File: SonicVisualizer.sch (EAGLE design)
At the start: 71 parts, among them U1 LMV324, U2 LMV324, U3 LMV324, U4 +12v, U5 +12v

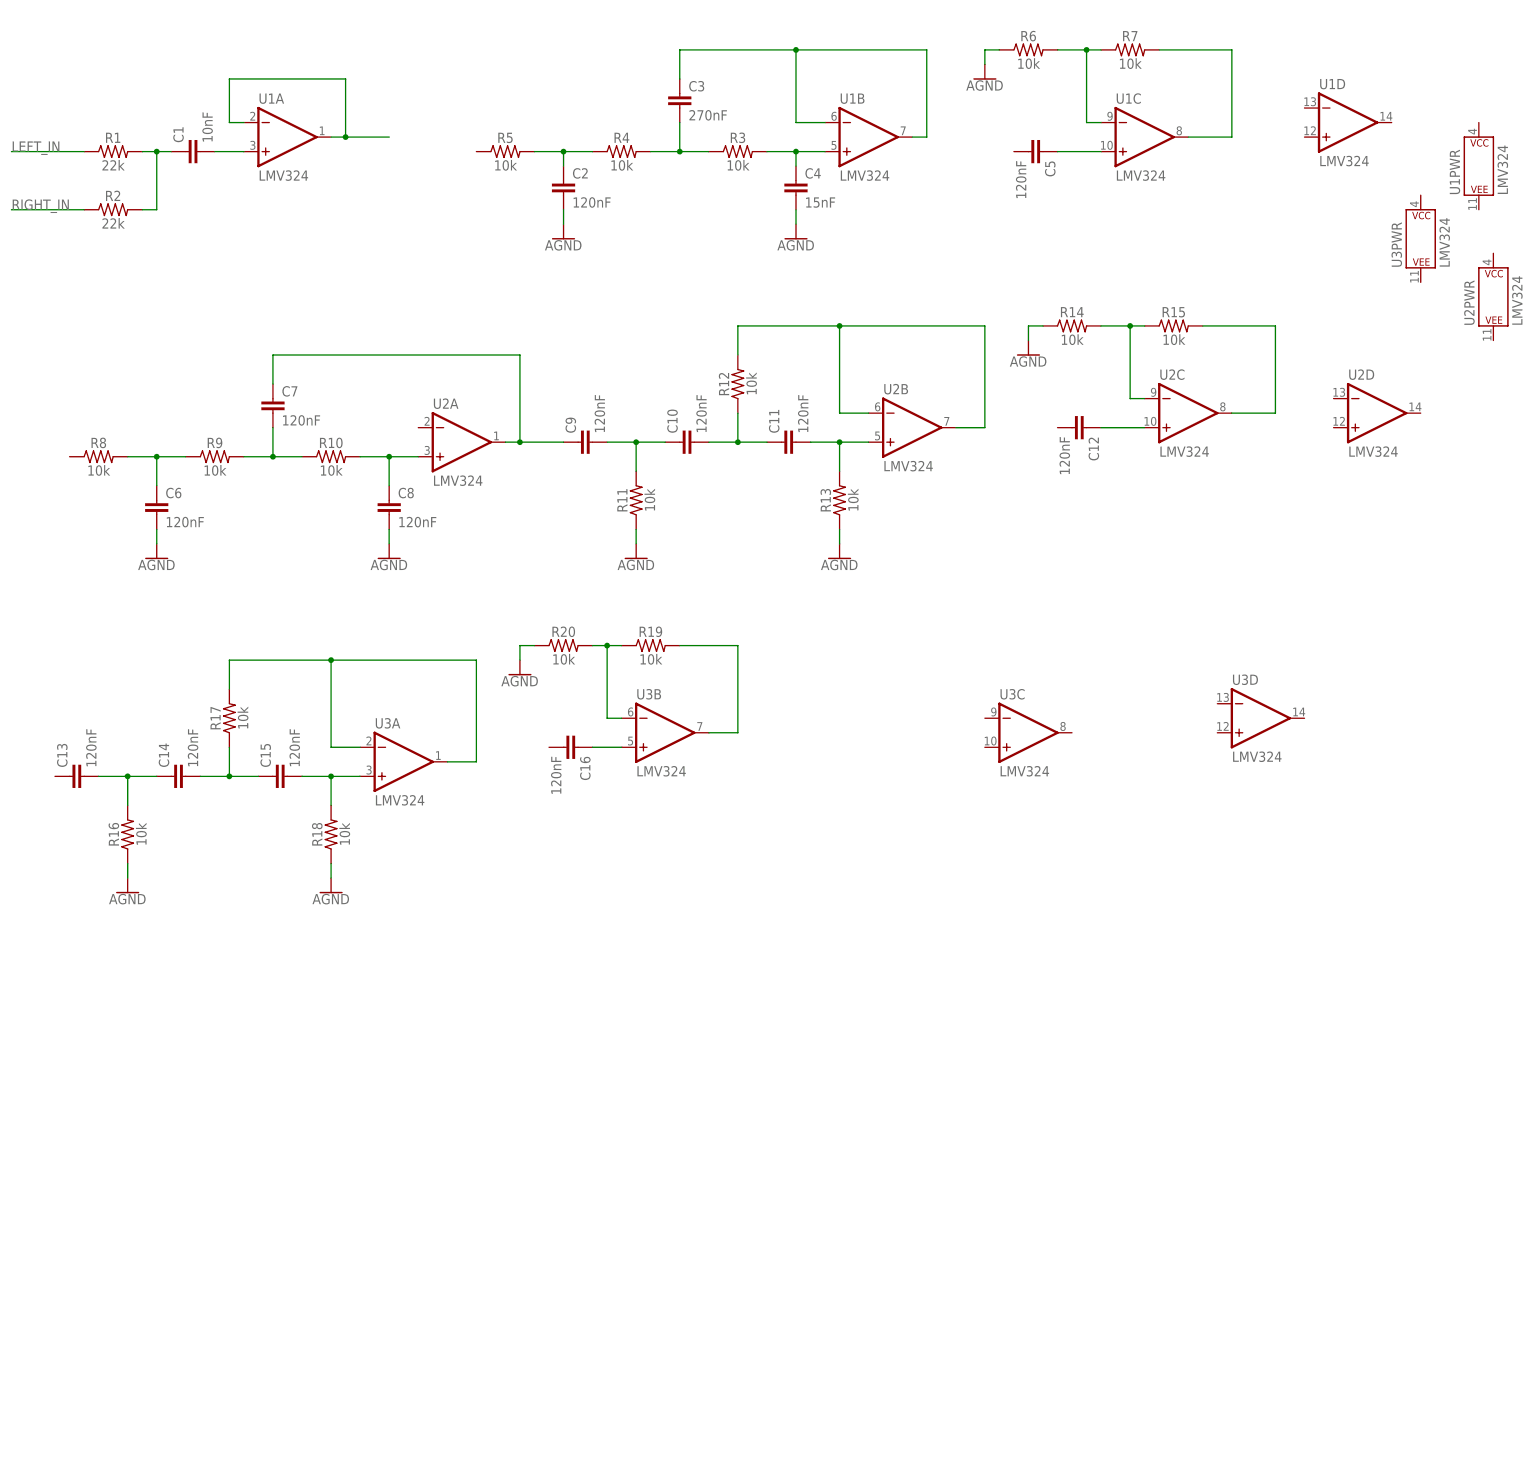
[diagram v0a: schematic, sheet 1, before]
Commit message: Compressed schematic and added envelope detect stage
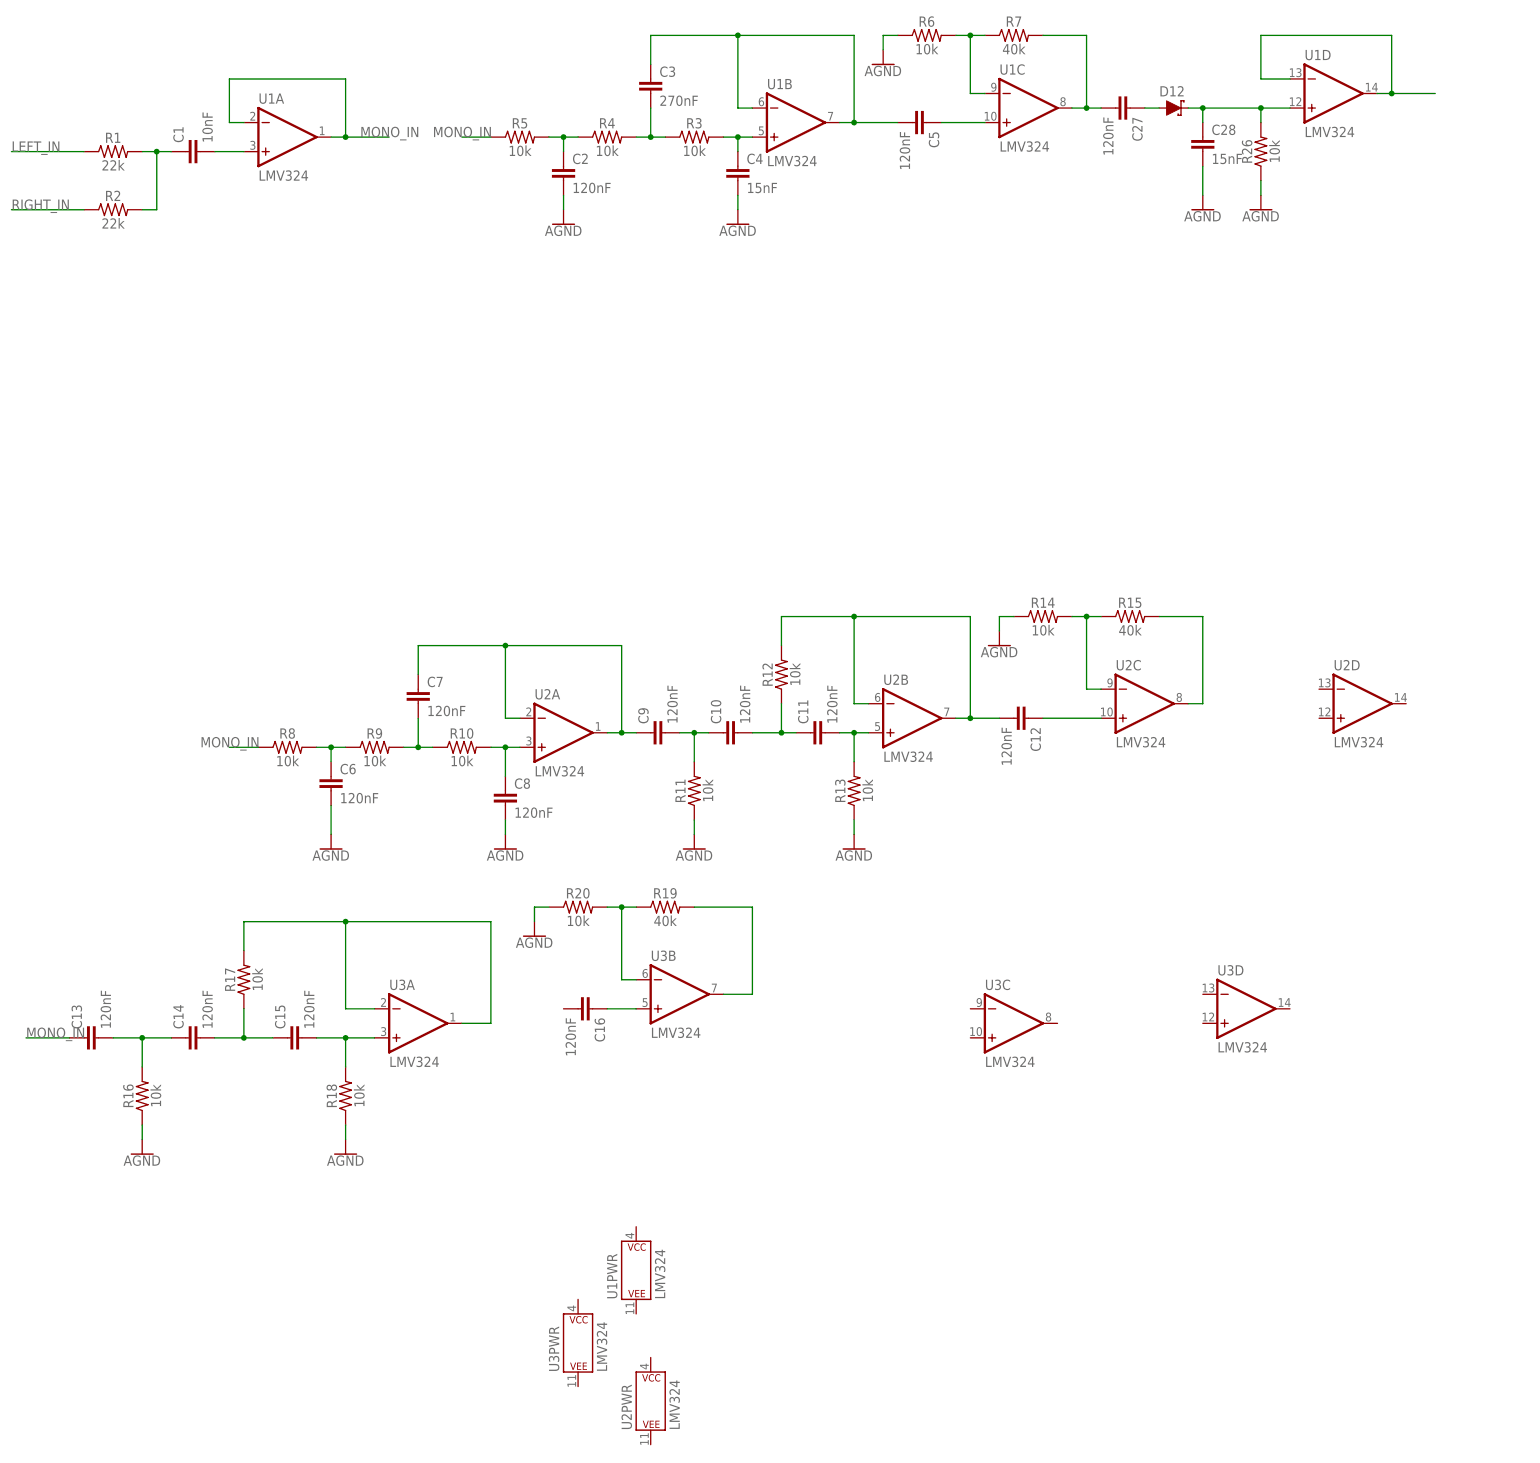
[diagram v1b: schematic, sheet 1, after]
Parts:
- added C27: 120nF, SparkFun-Capacitors:0.1UF-0603-25V-(+80/-20%)
- added C28: 15nF, SparkFun-Capacitors:0.1UF-0603-25V-(+80/-20%)
- added D12: DIODE-SCHOTTKY-SS14, SparkFun-DiscreteSemi:DIODE-SCHOTTKY-SS14
- added R26: 10k, SparkFun-Resistors:10KOHM-0603-1/10W-1%
- R15, R19, R7: value 10k -> 40k
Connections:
- new net MONO_IN: C13.1, R5.1, R8.1, U1A.-IN, U1A.OUT
- new net N$30: C28.1, D12.C, R26.2, U1D.+IN
- new net N$31: U1D.-IN, U1D.OUT
- net AGND: now also C28.2, R26.1
- net N$10: now also C27.2
- net N$11: now also U2A.-IN
- net N$18: now also C12.2
- net N$3: now also C27.1, D12.A; no longer U1A.-IN, U1A.OUT
- net N$7: now also C5.2
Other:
- moved on the sheet: C10, C11, C12, C13, C14, C15, C16, C2, C3, C4, C5, C6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

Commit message: Added final stage, general touch up.
Still needs quite a bit of work, but general idea is there.
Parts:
- added C29, C31, C33: 120nF, SparkFun-Capacitors:0.1UF-0603-25V-(+80/-20%)
- added C30, C32: 100nF, SparkFun-Capacitors:0.1UF-0603-25V-(+80/-20%)
- added C34: 0.1uF, SparkFun-Capacitors:0.1UF-0603-25V-(+80/-20%)
- added D13, D14: DIODE-SCHOTTKY-SS14, SparkFun-DiscreteSemi:DIODE-SCHOTTKY-SS14
- added J1: AUDIO_JACK_3.5MM_SMD, SparkFun-Connectors:AUDIO_JACK_3.5MM_SMD
- added J2: (no value), SparkFun-Connectors:CONN_04
- added Q1: \, SparkFun-DiscreteSemi:MOSFET_PCH-IRLML2244
- added Q2: MOSFET-NCH-2N7002PW, SparkFun-DiscreteSemi:MOSFET-NCH-2N7002PW
- added R27, R28, R33: 100k, SparkFun-Resistors:10KOHM-0603-1/10W-1%
- added R29: 100M, SparkFun-Resistors:10KOHM-0603-1/10W-1%
- added R30: 1M, SparkFun-Resistors:10KOHM-0603-1/10W-1%
- added R31: 510k, SparkFun-Resistors:10KOHM-0603-1/10W-1%
- added R32: 10k, SparkFun-Resistors:10KOHM-0603-1/10W-1%
- added U6: LTC6992, SonicVisualizer:LTC6992
- added VR1, VR2: 10k, SparkFun-Resistors:TRIMPOT-SMD-3MM-CLOSED-1/8W-20%
- C28: value 15nF -> 100nF
- R26: value 10k -> 500k
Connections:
- net N$31 renamed LOW_DET
- new net AC_HOT: U$18.P$1
- new net AC_NEUTRAL: TR1.2
- new net BLUE: J2.3
- new net GREEN: J2.2
- new net HIGH_DET: U3C.-IN, U3C.OUT
- new net MID_DET: U2D.-IN, U2D.OUT
- new net N$31: R29.2, U6.SET
- new net N$34: R30.2, R31.2, U6.DIV
- new net N$36: C29.1, D13.A
- new net N$37: C30.1, D13.C, R27.2, U2D.+IN
- new net N$38: C33.2, VR1.WIPER
- new net N$40: Q2.G, U6.OUT
- new net N$41: C31.1, D14.A
- new net N$42: C32.1, D14.C, R28.2, U3C.+IN
- new net N$43: R32.1, VR1.CCW
- new net N$44: C33.1, U6.MOD, VR2.WIPER
- new net N$45: R32.2
- new net N$46: Q1.G, Q2.D, R33.1
- new net N$47: RT1.2, TR1.1
- new net N$48: S1.P, U$18.P$2
- new net N$49: RT1.1, S1.O
- new net RED: J2.1, Q1.S
- net AGND: now also C30.2, C32.2, C34.2, J1.SLEEVE, R27.1, R28.1, R29.1, R30.1, U6.GND, VR1.CW, VR2.CW
- net GND: now also Q2.S
- net LEFT_IN: now also J1.RING
- net N$21: now also C29.2
- net N$25: now also C16.2
- net N$28: now also C31.2
- net RIGHT_IN: now also J1.TIP
- net V+: now also Q1.D, R33.2
- net V-: now also J2.4
- net VCC: now also C34.1, R31.1, U6.V+, VR2.CCW
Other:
- moved on the sheet: C1, C10, C11, C12, C13, C14, C15, C16, C17, C18, C19, C2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

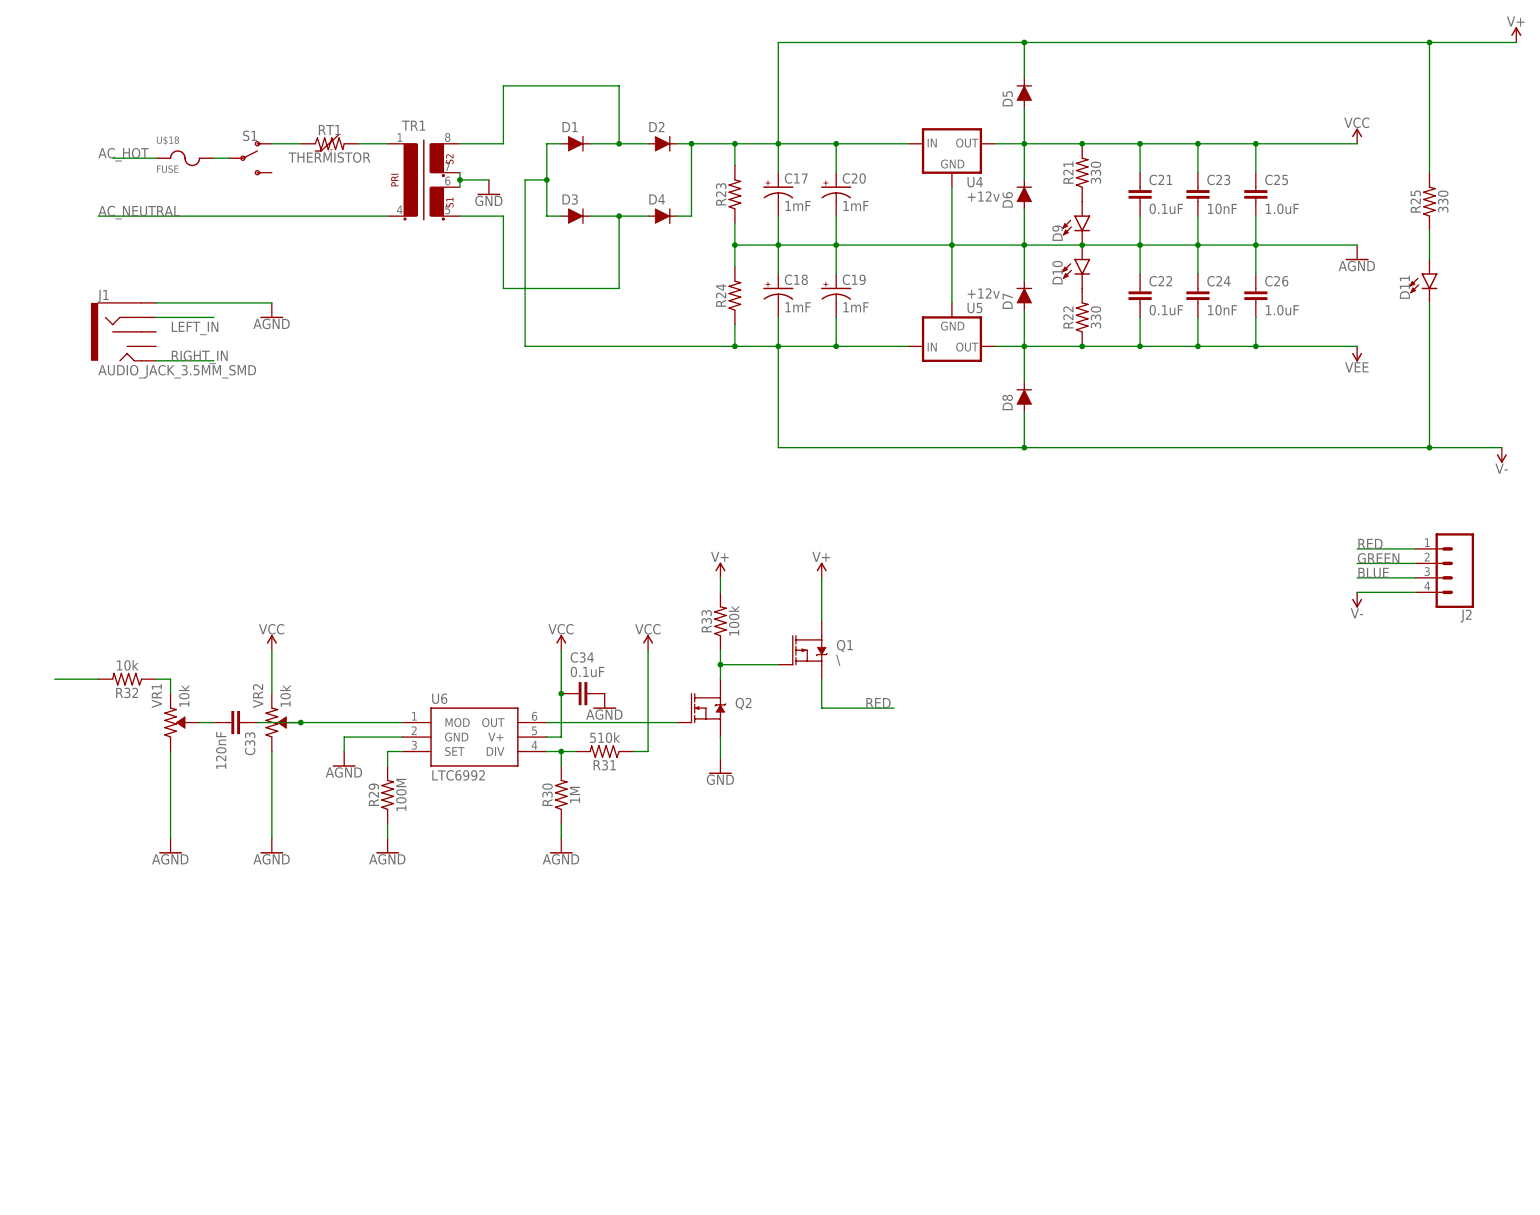
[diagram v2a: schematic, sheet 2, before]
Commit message: Finished all output stages, general touch up on power supplies, connectors, etc.
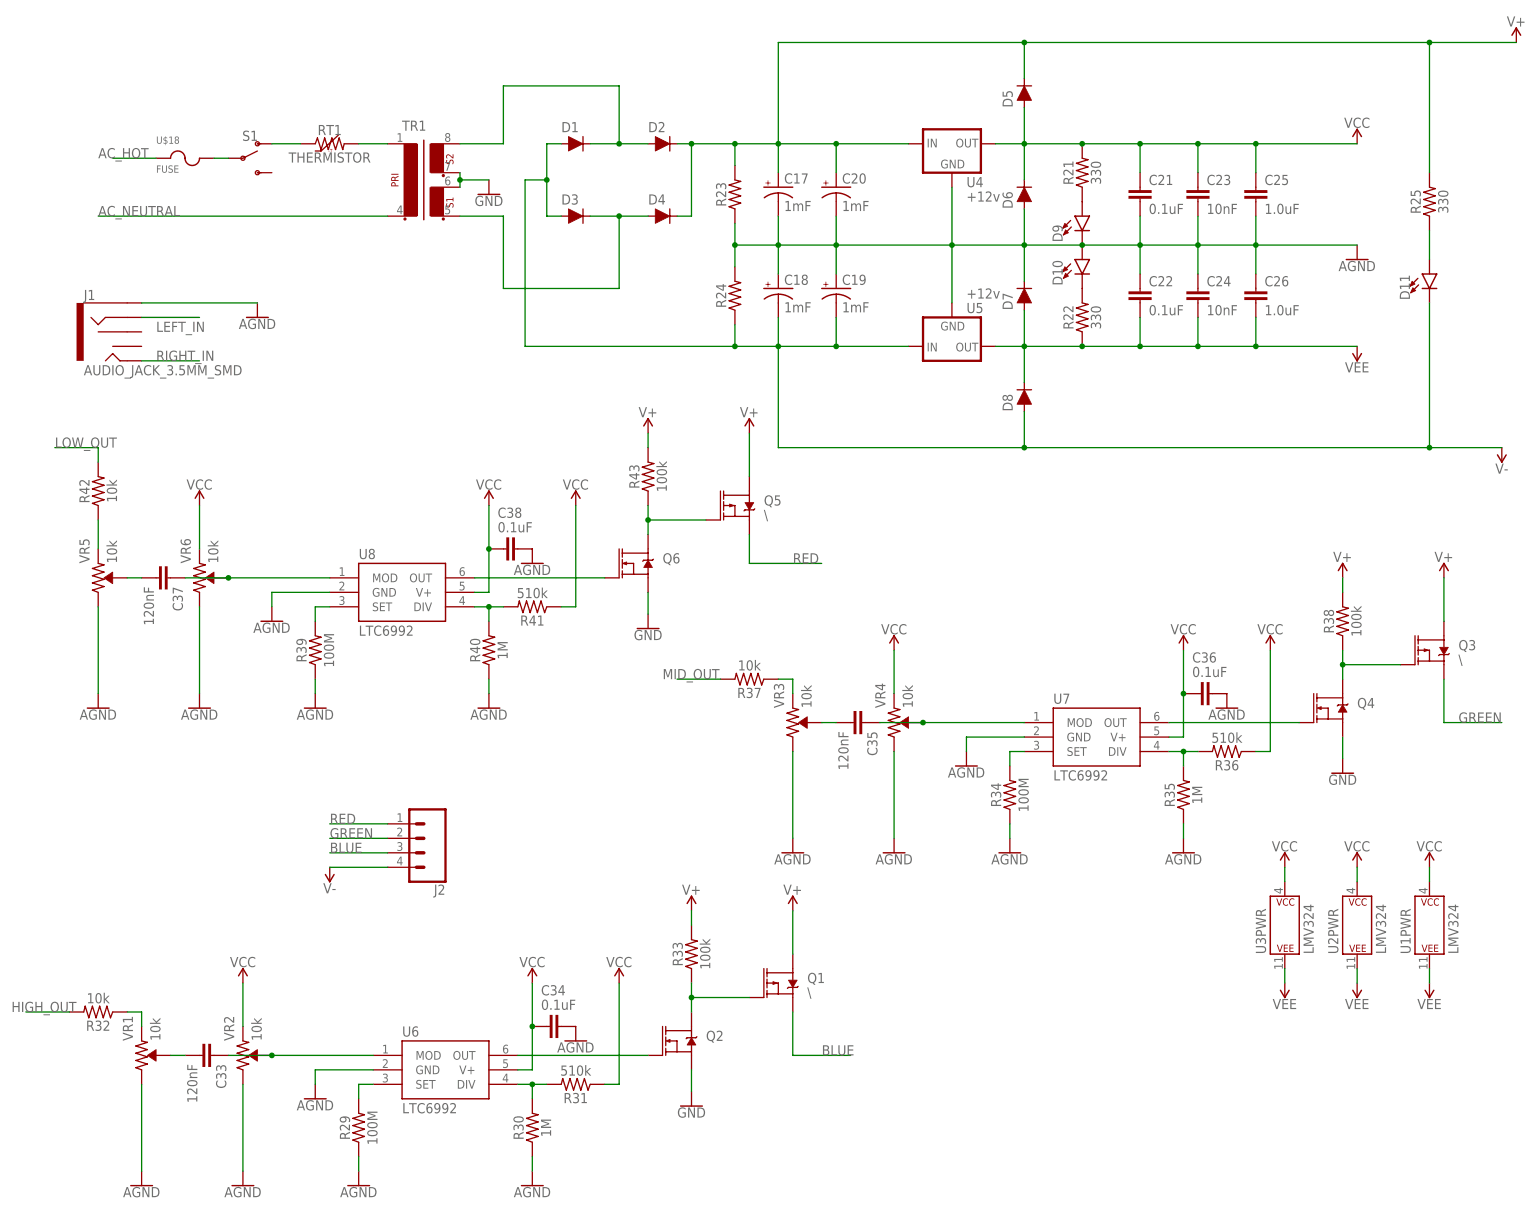
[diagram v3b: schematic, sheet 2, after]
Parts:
- added C35, C37: 120nF, SparkFun-Capacitors:0.1UF-0603-25V-(+80/-20%)
- added C36, C38: 0.1uF, SparkFun-Capacitors:0.1UF-0603-25V-(+80/-20%)
- added Q3, Q5: \, SparkFun-DiscreteSemi:MOSFET_PCH-IRLML2244
- added Q4, Q6: MOSFET-NCH-2N7002PW, SparkFun-DiscreteSemi:MOSFET-NCH-2N7002PW
- added R34, R39: 100M, SparkFun-Resistors:10KOHM-0603-1/10W-1%
- added R35, R40: 1M, SparkFun-Resistors:10KOHM-0603-1/10W-1%
- added R36, R41: 510k, SparkFun-Resistors:10KOHM-0603-1/10W-1%
- added R37, R42: 10k, SparkFun-Resistors:10KOHM-0603-1/10W-1%
- added R38, R43: 100k, SparkFun-Resistors:10KOHM-0603-1/10W-1%
- added U7, U8: LTC6992, SonicVisualizer:LTC6992
- added VR3, VR4, VR5, VR6: 10k, SparkFun-Resistors:TRIMPOT-SMD-3MM-CLOSED-1/8W-20%
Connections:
- net N$45 renamed HIGH_OUT
- new net LOW_OUT: R42.2
- new net MID_OUT: R37.2
- new net N$50: R34.2, U7.SET
- new net N$51: R35.2, R36.2, U7.DIV
- new net N$52: C35.1, U7.MOD, VR4.WIPER
- new net N$53: C35.2, VR3.WIPER
- new net N$54: R37.1, VR3.CCW
- new net N$56: Q4.G, U7.OUT
- new net N$57: Q3.G, Q4.D, R38.1
- new net N$58: R39.2, U8.SET
- new net N$59: R40.2, R41.2, U8.DIV
- new net N$60: C37.1, U8.MOD, VR6.WIPER
- new net N$61: C37.2, VR5.WIPER
- new net N$62: R42.1, VR5.CCW
- new net N$64: Q6.G, U8.OUT
- new net N$65: Q5.G, Q6.D, R43.1
- net AGND: now also C36.2, C38.2, R34.1, R35.1, R39.1, R40.1, U3D.+IN, U3D.-IN, U3D.OUT, U7.GND, U8.GND, VR3.CW, VR4.CW, VR5.CW, VR6.CW
- net BLUE: now also Q1.S
- net GND: now also Q4.S, Q6.S
- net GREEN: now also Q3.S
- net RED: now also Q5.S; no longer Q1.S
- net V+: now also Q3.D, Q5.D, R38.2, R43.2
- net VCC: now also C36.1, C38.1, R36.1, R41.1, U1PWR.P$V+, U2PWR.P$V+, U3PWR.P$V+, U7.V+, U8.V+, VR4.CCW, VR6.CCW
- net VEE: now also U1PWR.P$V-, U2PWR.P$V-, U3PWR.P$V-
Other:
- moved on the sheet: C33, C34, J1, J2, Q1, Q2, R29, R30, R31, R32, R33, U6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
